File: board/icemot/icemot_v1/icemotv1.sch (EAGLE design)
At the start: 13 parts, among them U1 ICE40HX4K, U2 EFM32WG332FXXX-QFP64

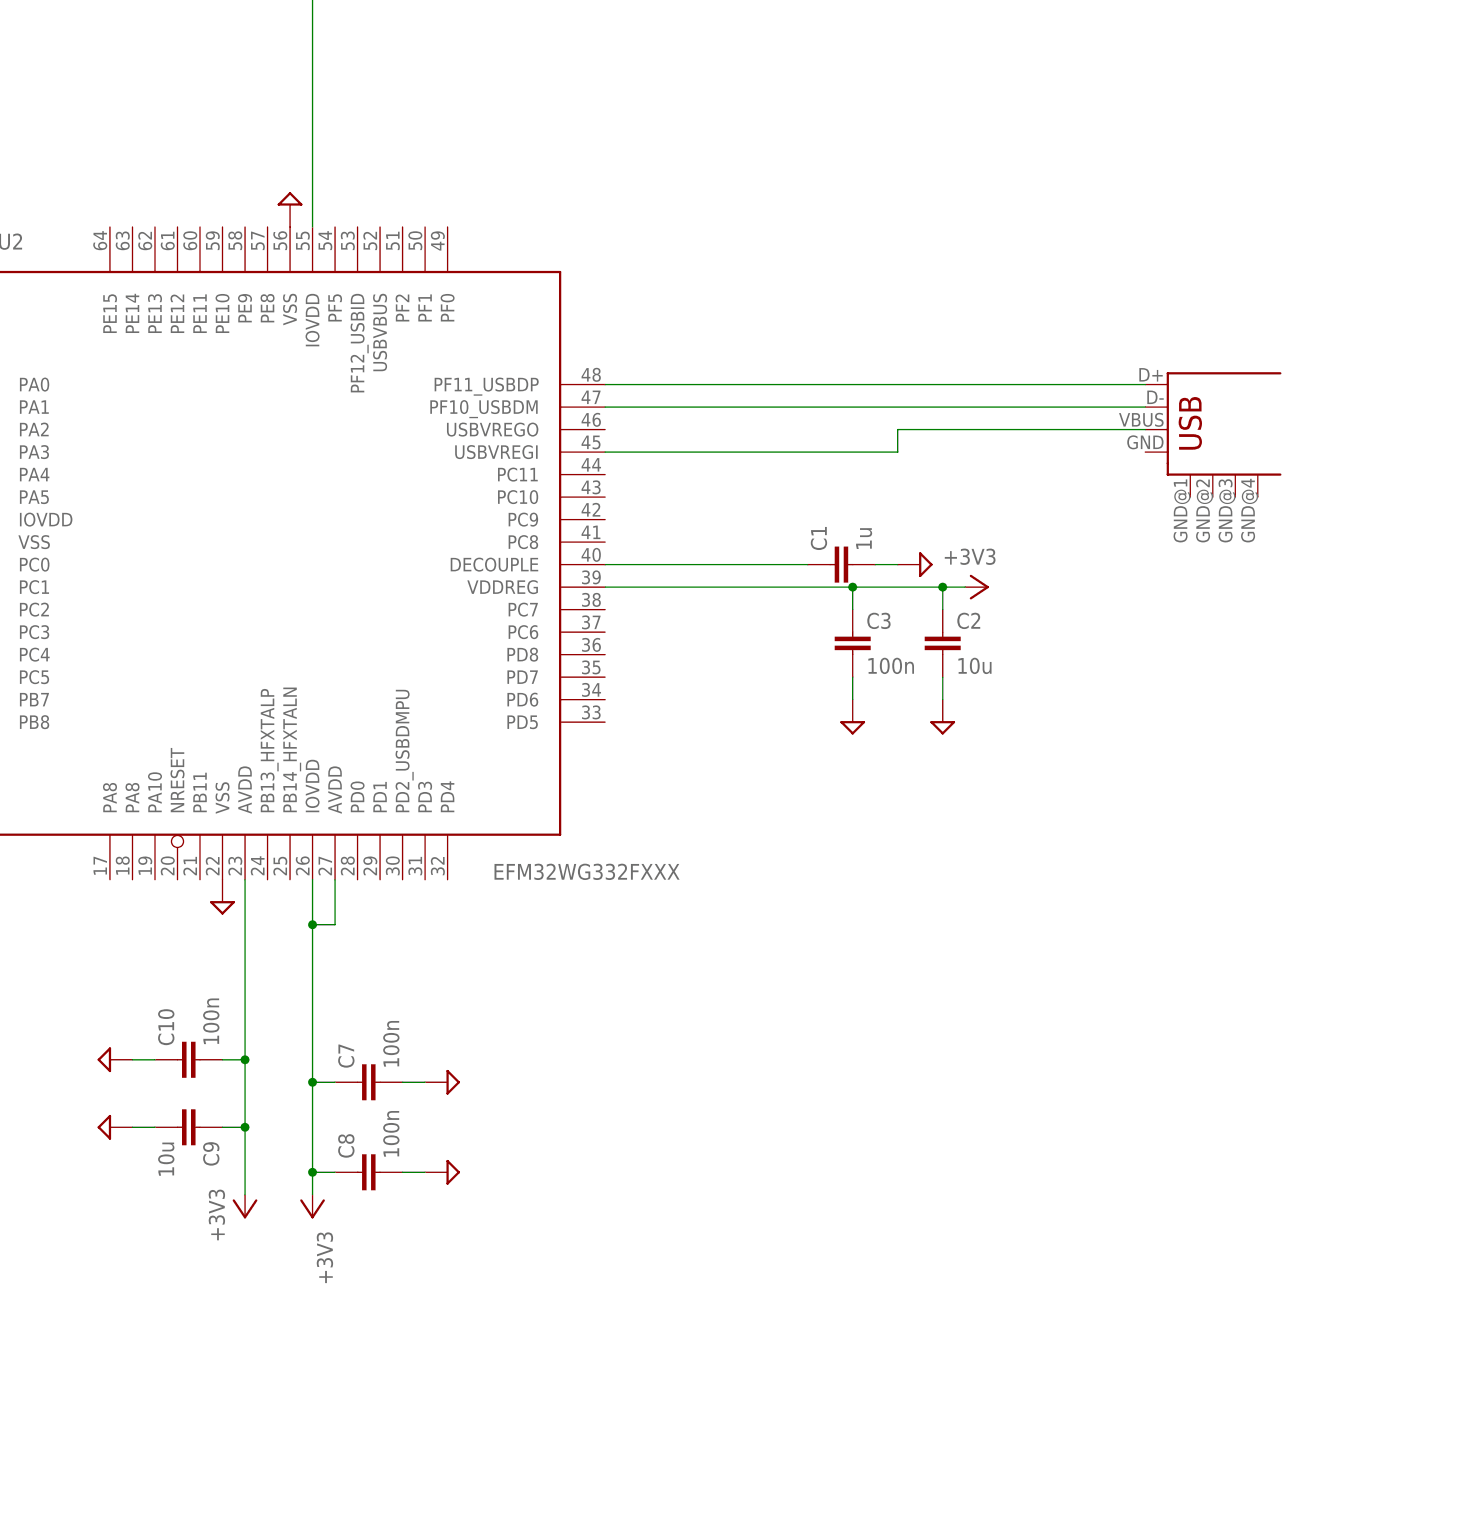
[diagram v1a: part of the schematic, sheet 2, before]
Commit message: added xtal, usb to be checked
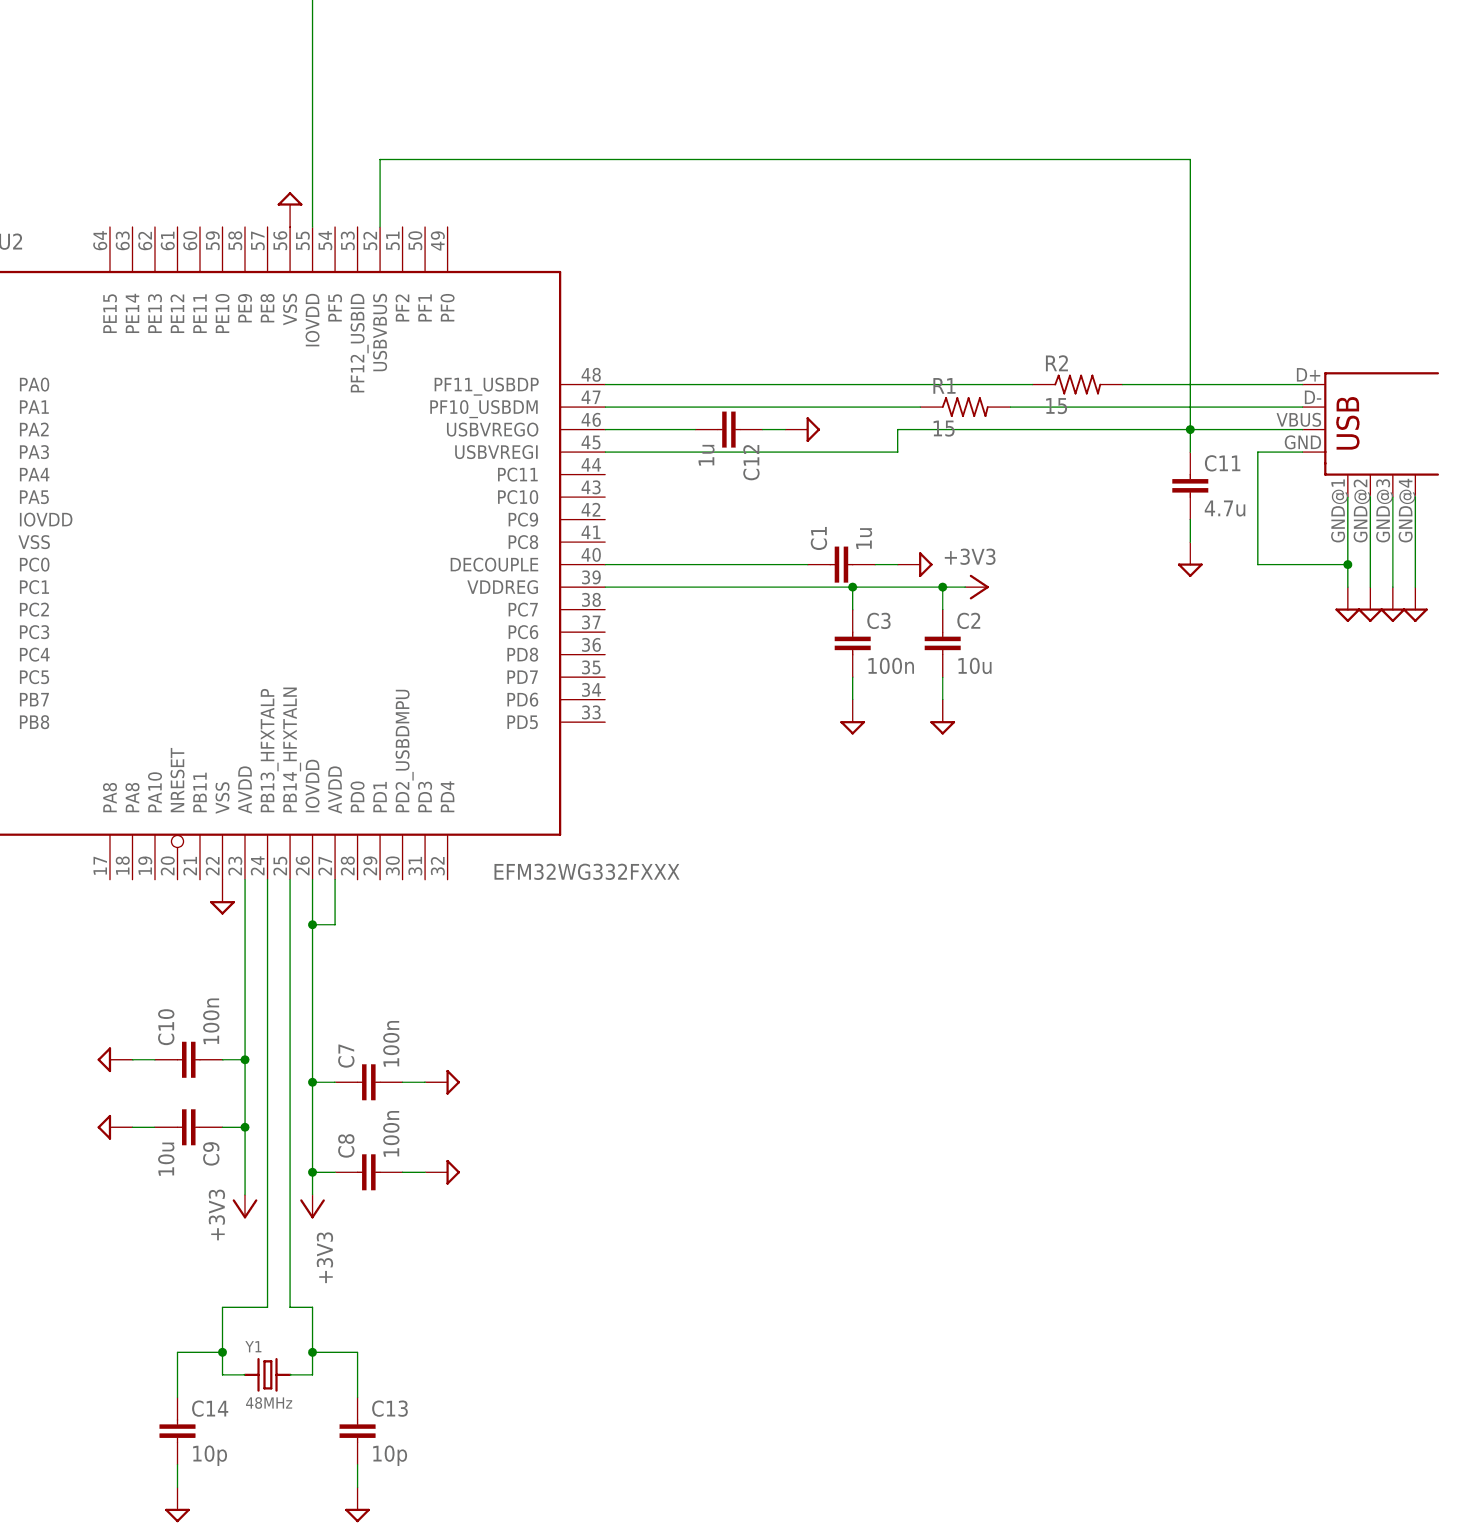
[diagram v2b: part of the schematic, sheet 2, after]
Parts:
- added C11: 4.7u, standard_passive:CAP_0805
- added C12: 1u, standard_passive:CAP_0603
- added C13, C14: 10p, standard_passive:CAP_0603
- added R1, R2: 15, standard_passive:RES_0603
- added Y1: 48MHz, xtals:CRYSTAL.3.2X2.5MM
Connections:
- new net N$5: C12.2, U2.USBVREGO@46
- new net N$6: R2.2, U$1.D+
- new net N$7: R2.1, U2.PF11_USBDP@48
- new net N$8: C13.1, U2.PB14_HFXTALN@25, Y1.2
- new net N$9: C14.1, U2.PB13_HFXTALP@24, Y1.1
- net GND: now also C11.2, C12.1, C13.2, C14.2, U$1.GND, U$1.GND@1, U$1.GND@2, U$1.GND@3, U$1.GND@4
- net N$2: now also R1.1, U2.PF10_USBDM@47; no longer U$1.D+, U2.PF11_USBDP@48
- net N$3: now also R1.2; no longer U2.PF10_USBDM@47
- net N$4: now also C11.1, U2.USBVBUS@52
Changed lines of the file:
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@@
 <part name="SUPPLY13" library="supply2" deviceset="GND" device=""/>
 <part name="U$1" library="usb-header" deviceset="USB-SHIELD" device=""/>
+<part name="SUPPLY14" library="supply2" deviceset="GND" device=""/>
+<part name="SUPPLY15" library="supply2" deviceset="GND" device=""/>
+<part name="SUPPLY16" library="supply2" deviceset="GND" device=""/>
+<part name="SUPPLY17" library="supply2" deviceset="GND" device=""/>
+<part name="C11" library="standard_passive" deviceset="CAP_0805" device="" value="4.7u"/>
+<part name="SUPPLY18" library="supply2" deviceset="GND" device=""/>
+<part name="C12" library="standard_passive" deviceset="CAP_0603" device="" value="1u"/>
+<part name="SUPPLY19" library="supply2" deviceset="GND" device=""/>
+<part name="R1" library="standard_passive" deviceset="RES_0603" device="" value="15"/>
+<part name="R2" library="standard_passive" deviceset="RES_0603" device="" value="15"/>
+<part name="Y1" library="xtals" deviceset="CRYSTAL" device=".3.2X2.5MM" value="48MHz"/>
+<part name="C13" library="standard_passive" deviceset="CAP_0603" device="" value="10p"/>
+<part name="C14" library="standard_passive" deviceset="CAP_0603" device="" value="10p"/>
+<part name="SUPPLY20" library="supply2" deviceset="GND" device=""/>
+<part name="SUPPLY21" library="supply2" deviceset="GND" device=""/>
 </parts>
 <sheets>
@@
 <attribute name="VALUE" x="174.625" y="67.945" size="1.778" layer="96" rot="R270" display="off"/>
 </instance>
-<instance part="U$1" gate="USB" x="299.72" y="144.78"/>
+<instance part="U$1" gate="USB" x="317.5" y="144.78"/>
+<instance part="SUPPLY14" gate="GND" x="317.5" y="124.46" smashed="yes">
+<attribute name="VALUE" x="315.595" y="121.285" size="1.778" layer="96" display="off"/>
+</instance>
+<instance part="SUPPLY15" gate="GND" x="322.58" y="124.46" smashed="yes">
+<attribute name="VALUE" x="320.675" y="121.285" size="1.778" layer="96" display="off"/>
+</instance>
+<instance part="SUPPLY16" gate="GND" x="320.04" y="124.46" smashed="yes">
+<attribute name="VALUE" x="318.135" y="121.285" size="1.778" layer="96" display="off"/>
+</instance>
+<instance part="SUPPLY17" gate="GND" x="325.12" y="124.46" smashed="yes">
+<attribute name="VALUE" x="323.215" y="121.285" size="1.778" layer="96" display="off"/>
+</instance>
+<instance part="C11" gate="G$1" x="299.72" y="139.7"/>
+<instance part="SUPPLY18" gate="GND" x="299.72" y="129.54" smashed="yes">
+<attribute name="VALUE" x="297.815" y="126.365" size="1.778" layer="96" display="off"/>
+</instance>
+<instance part="C12" gate="G$1" x="248.92" y="144.78" rot="R270"/>
+<instance part="SUPPLY19" gate="GND" x="256.54" y="144.78" smashed="yes" rot="R90">
+<attribute name="VALUE" x="259.715" y="142.875" size="1.778" layer="96" rot="R90" display="off"/>
+</instance>
+<instance part="R1" gate="G$1" x="274.32" y="147.32"/>
+<instance part="R2" gate="G$1" x="287.02" y="149.86"/>
+<instance part="Y1" gate="G$1" x="195.58" y="38.1"/>
+<instance part="C13" gate="G$1" x="205.74" y="33.02"/>
+<instance part="C14" gate="G$1" x="185.42" y="33.02"/>
+<instance part="SUPPLY20" gate="GND" x="205.74" y="22.86" smashed="yes">
+<attribute name="VALUE" x="203.835" y="19.685" size="1.778" layer="96" display="off"/>
+</instance>
+<instance part="SUPPLY21" gate="GND" x="185.42" y="22.86" smashed="yes">
+<attribute name="VALUE" x="183.515" y="19.685" size="1.778" layer="96" display="off"/>
+</instance>
 </instances>
 <busses>
@@
 <pinref part="C9" gate="G$1" pin="2"/>
 <wire x1="180.34" y1="66.04" x2="182.88" y2="66.04" width="0.1524" layer="91"/>
+</segment>
+<segment>
+<pinref part="U$1" gate="USB" pin="GND@1"/>
+<pinref part="SUPPLY14" gate="GND" pin="GND"/>
+<wire x1="317.5" y1="137.16" x2="317.5" y2="129.54" width="0.1524" layer="91"/>
+<pinref part="U$1" gate="USB" pin="GND"/>
+<wire x1="317.5" y1="129.54" x2="317.5" y2="127" width="0.1524" layer="91"/>
+<wire x1="312.42" y1="142.24" x2="307.34" y2="142.24" width="0.1524" layer="91"/>
+<wire x1="307.34" y1="142.24" x2="307.34" y2="129.54" width="0.1524" layer="91"/>
+<wire x1="307.34" y1="129.54" x2="317.5" y2="129.54" width="0.1524" layer="91"/>
+<junction x="317.5" y="129.54"/>
+</segment>
+<segment>
+<pinref part="U$1" gate="USB" pin="GND@2"/>
+<pinref part="SUPPLY16" gate="GND" pin="GND"/>
+<wire x1="320.04" y1="137.16" x2="320.04" y2="127" width="0.1524" layer="91"/>
+</segment>
+<segment>
+<pinref part="U$1" gate="USB" pin="GND@3"/>
+<pinref part="SUPPLY15" gate="GND" pin="GND"/>
+<wire x1="322.58" y1="137.16" x2="322.58" y2="127" width="0.1524" layer="91"/>
+</segment>
+<segment>
+<pinref part="U$1" gate="USB" pin="GND@4"/>
+<pinref part="SUPPLY17" gate="GND" pin="GND"/>
+<wire x1="325.12" y1="137.16" x2="325.12" y2="127" width="0.1524" layer="91"/>
+</segment>
+<segment>
+<pinref part="C11" gate="G$1" pin="2"/>
+<pinref part="SUPPLY18" gate="GND" pin="GND"/>
+<wire x1="299.72" y1="134.62" x2="299.72" y2="132.08" width="0.1524" layer="91"/>
+</segment>
+<segment>
+<pinref part="C12" gate="G$1" pin="1"/>
+<pinref part="SUPPLY19" gate="GND" pin="GND"/>
+<wire x1="251.46" y1="144.78" x2="254" y2="144.78" width="0.1524" layer="91"/>
+</segment>
+<segment>
+<pinref part="C14" gate="G$1" pin="2"/>
+<pinref part="SUPPLY21" gate="GND" pin="GND"/>
+<wire x1="185.42" y1="27.94" x2="185.42" y2="25.4" width="0.1524" layer="91"/>
+</segment>
+<segment>
+<pinref part="C13" gate="G$1" pin="2"/>
+<pinref part="SUPPLY20" gate="GND" pin="GND"/>
+<wire x1="205.74" y1="27.94" x2="205.74" y2="25.4" width="0.1524" layer="91"/>
 </segment>
 </net>
@@
 </segment>
 </net>
-<net name="N$2" class="0">
-<segment>
-<pinref part="U$1" gate="USB" pin="D+"/>
-<pinref part="U2" gate="F" pin="PF11_USBDP@48"/>
-<wire x1="294.64" y1="149.86" x2="233.68" y2="149.86" width="0.1524" layer="91"/>
-</segment>
-</net>
-<net name="N$3" class="0">
-<segment>
-<pinref part="U$1" gate="USB" pin="D-"/>
-<pinref part="U2" gate="F" pin="PF10_USBDM@47"/>
-<wire x1="294.64" y1="147.32" x2="233.68" y2="147.32" width="0.1524" layer="91"/>
-</segment>
-</net>
 <net name="N$4" class="0">
 <segment>
 <pinref part="U$1" gate="USB" pin="VBUS"/>
-<wire x1="294.64" y1="144.78" x2="266.7" y2="144.78" width="0.1524" layer="91"/>
+<wire x1="312.42" y1="144.78" x2="299.72" y2="144.78" width="0.1524" layer="91"/>
+<wire x1="299.72" y1="144.78" x2="266.7" y2="144.78" width="0.1524" layer="91"/>
 <wire x1="266.7" y1="144.78" x2="266.7" y2="142.24" width="0.1524" layer="91"/>
 <pinref part="U2" gate="F" pin="USBVREGI@45"/>
 <wire x1="266.7" y1="142.24" x2="233.68" y2="142.24" width="0.1524" layer="91"/>
-</segment>
-</net>
+<pinref part="C11" gate="G$1" pin="1"/>
+<wire x1="299.72" y1="142.24" x2="299.72" y2="144.78" width="0.1524" layer="91"/>
+<junction x="299.72" y="144.78"/>
+<wire x1="299.72" y1="144.78" x2="299.72" y2="175.26" width="0.1524" layer="91"/>
+<pinref part="U2" gate="F" pin="USBVBUS@52"/>
+<wire x1="299.72" y1="175.26" x2="208.28" y2="175.26" width="0.1524" layer="91"/>
+<wire x1="208.28" y1="175.26" x2="208.28" y2="167.64" width="0.1524" layer="91"/>
+</segment>
+</net>
+<net name="N$5" class="0">
+<segment>
+<pinref part="U2" gate="F" pin="USBVREGO@46"/>
+<pinref part="C12" gate="G$1" pin="2"/>
+<wire x1="233.68" y1="144.78" x2="243.84" y2="144.78" width="0.1524" layer="91"/>
+</segment>
+</net>
+<net name="N$2" class="0">
+<segment>
+<pinref part="U2" gate="F" pin="PF10_USBDM@47"/>
+<pinref part="R1" gate="G$1" pin="1"/>
+<wire x1="233.68" y1="147.32" x2="269.24" y2="147.32" width="0.1524" layer="91"/>
+</segment>
+</net>
+<net name="N$3" class="0">
+<segment>
+<pinref part="R1" gate="G$1" pin="2"/>
+<pinref part="U$1" gate="USB" pin="D-"/>
+<wire x1="279.4" y1="147.32" x2="312.42" y2="147.32" width="0.1524" layer="91"/>
+</segment>
+</net>
+<net name="N$6" class="0">
+<segment>
+<pinref part="U$1" gate="USB" pin="D+"/>
+<pinref part="R2" gate="G$1" pin="2"/>
+<wire x1="312.42" y1="149.86" x2="292.1" y2="149.86" width="0.1524" layer="91"/>
+</segment>
+</net>
+<net name="N$7" class="0">
+<segment>
+<pinref part="R2" gate="G$1" pin="1"/>
+<pinref part="U2" gate="F" pin="PF11_USBDP@48"/>
+<wire x1="281.94" y1="149.86" x2="233.68" y2="149.86" width="0.1524" layer="91"/>
+</segment>
+</net>
+<net name="N$8" class="0">
+<segment>
+<pinref part="Y1" gate="G$1" pin="2"/>
+<wire x1="198.12" y1="38.1" x2="200.66" y2="38.1" width="0.1524" layer="91"/>
+<wire x1="200.66" y1="38.1" x2="200.66" y2="40.64" width="0.1524" layer="91"/>
+<wire x1="200.66" y1="40.64" x2="200.66" y2="45.72" width="0.1524" layer="91"/>
+<wire x1="200.66" y1="45.72" x2="198.12" y2="45.72" width="0.1524" layer="91"/>
+<pinref part="U2" gate="F" pin="PB14_HFXTALN@25"/>
+<wire x1="198.12" y1="45.72" x2="198.12" y2="93.98" width="0.1524" layer="91"/>
+<pinref part="C13" gate="G$1" pin="1"/>
+<wire x1="205.74" y1="35.56" x2="205.74" y2="40.64" width="0.1524" layer="91"/>
+<wire x1="205.74" y1="40.64" x2="200.66" y2="40.64" width="0.1524" layer="91"/>
+<junction x="200.66" y="40.64"/>
+</segment>
+</net>
+<net name="N$9" class="0">
+<segment>
+<pinref part="Y1" gate="G$1" pin="1"/>
+<wire x1="193.04" y1="38.1" x2="190.5" y2="38.1" width="0.1524" layer="91"/>
+<wire x1="190.5" y1="38.1" x2="190.5" y2="40.64" width="0.1524" layer="91"/>
+<wire x1="190.5" y1="40.64" x2="190.5" y2="45.72" width="0.1524" layer="91"/>
+<wire x1="190.5" y1="45.72" x2="195.58" y2="45.72" width="0.1524" layer="91"/>
+<pinref part="U2" gate="F" pin="PB13_HFXTALP@24"/>
+<wire x1="195.58" y1="45.72" x2="195.58" y2="93.98" width="0.1524" layer="91"/>
+<pinref part="C14" gate="G$1" pin="1"/>
+<wire x1="185.42" y1="35.56" x2="185.42" y2="40.64" width="0.1524" layer="91"/>
+<wire x1="185.42" y1="40.64" x2="190.5" y2="40.64" width="0.1524" layer="91"/>
+<junction x="190.5" y="40.64"/>
+</segment>
+</net>
